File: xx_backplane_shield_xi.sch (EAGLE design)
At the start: 31 parts, among them U7 LM2678

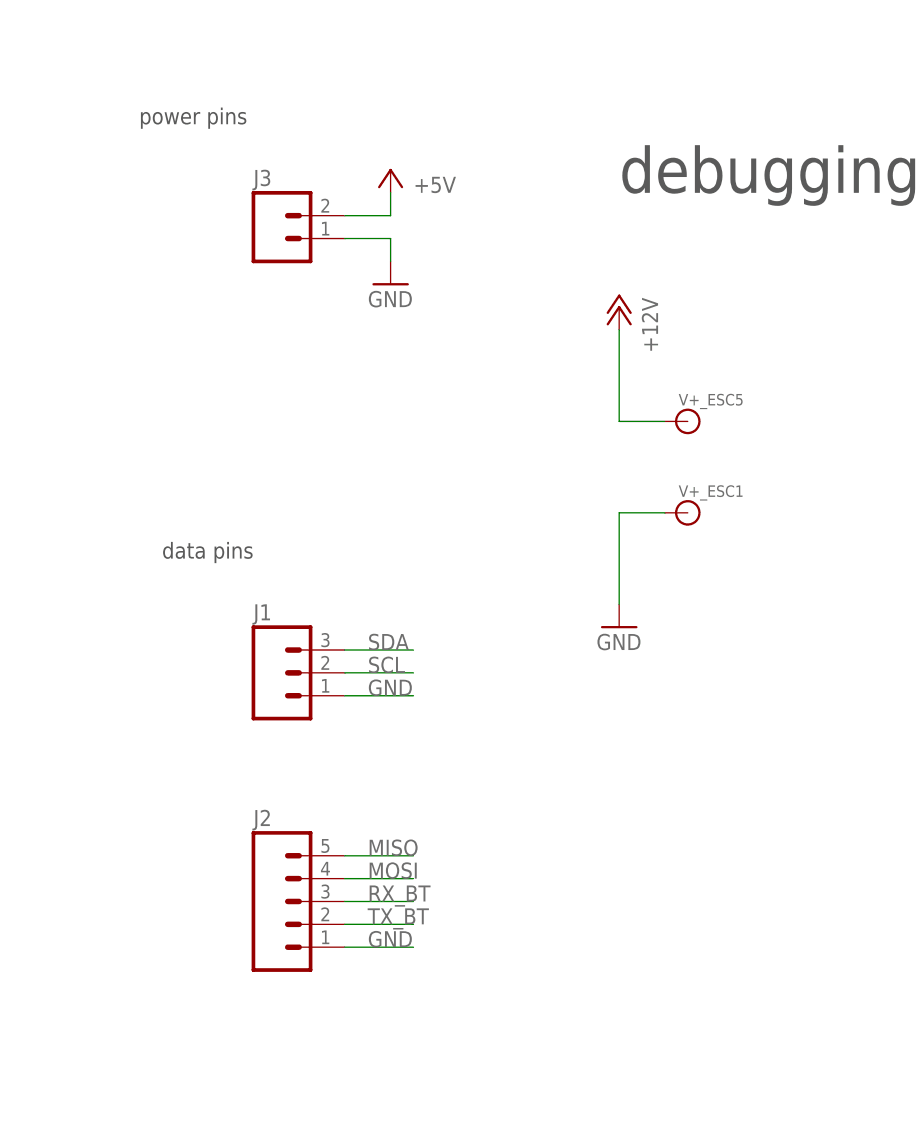
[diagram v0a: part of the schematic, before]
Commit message: Cleaning up eagle file and renaming board name
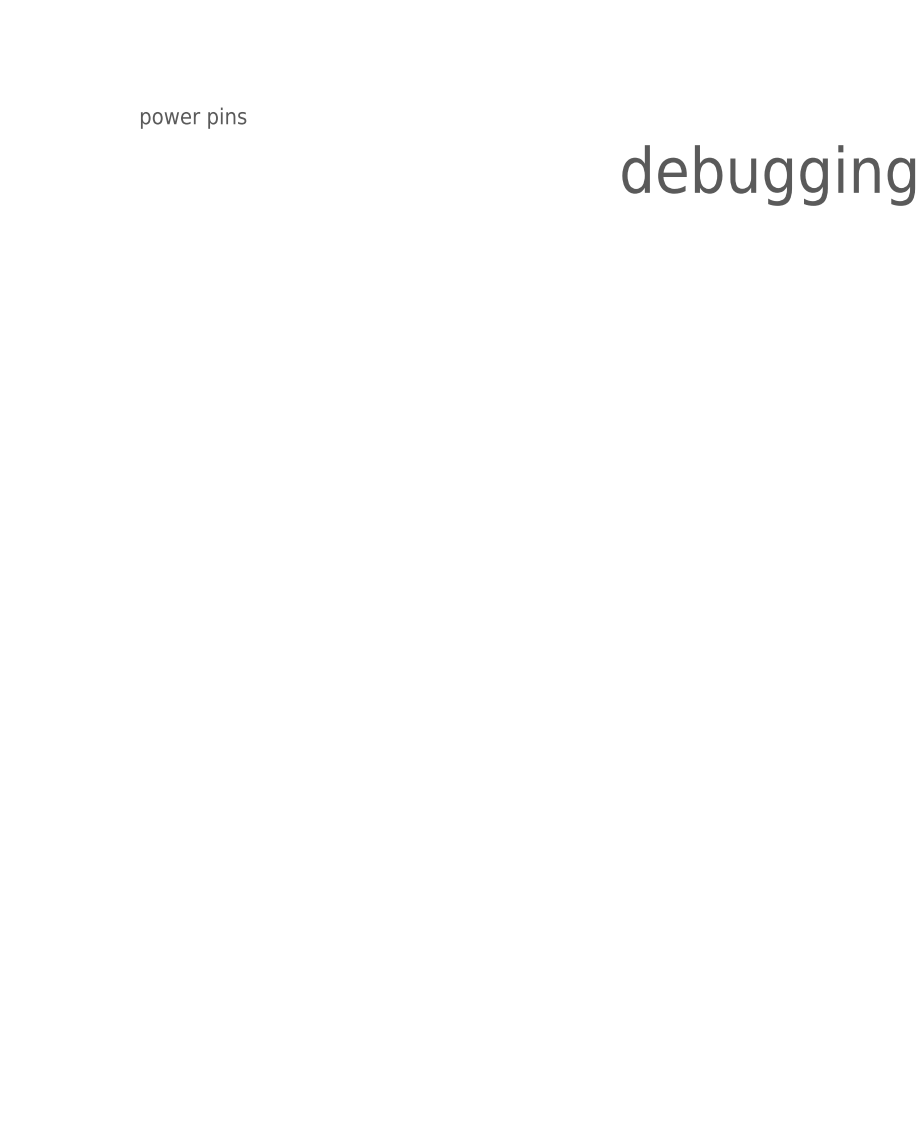
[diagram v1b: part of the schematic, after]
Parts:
- removed J1: (no value), SparkFun-Connectors:M03PTH
- removed J2: (no value), SparkFun-Connectors:M05PTH
- removed J3: (no value), SparkFun-Connectors:M02PTH
- removed V+_ESC1, V+_ESC5: (no value), SparkFun-Connectors:BANANA_CONN
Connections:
- removed net RX_BT: J2.3
- removed net TX_BT: J2.2
- net +12V: no longer V+_ESC5.1
- net +5V: no longer J3.2
- net GND: no longer J1.1, J2.1, J3.1, V+_ESC1.1
- net MISO: no longer J2.5
- net MOSI: no longer J2.4
- net SCL: no longer J1.2
- net SDA: no longer J1.3
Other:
- note removed: "data pins"
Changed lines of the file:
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@@
 <part name="GND19" library="SparkFun-Aesthetics" deviceset="GND" device=""/>
 <part name="P+3" library="supply1" deviceset="+12V" device=""/>
-<part name="J1" library="SparkFun-Connectors" deviceset="M03" device="PTH"/>
 <part name="FRAME5" library="frames" deviceset="FRAME_A_L" device=""/>
-<part name="J2" library="SparkFun-Connectors" deviceset="M05" device="PTH"/>
-<part name="J3" library="SparkFun-Connectors" deviceset="M02" device="PTH"/>
-<part name="P+8" library="supply1" deviceset="+5V" device=""/>
-<part name="GND25" library="SparkFun-Aesthetics" deviceset="GND" device=""/>
 <part name="C7" library="SparkFun-Passives" deviceset="CAP" device="0603-CAP" value="0.1u"/>
 <part name="GND29" library="SparkFun-Aesthetics" deviceset="GND" device=""/>
@@
 <part name="R14" library="resistor" deviceset="R-US_" device="R0603" value="330"/>
 <part name="GND33" library="SparkFun-Aesthetics" deviceset="GND" device=""/>
-<part name="P+10" library="supply1" deviceset="+12V" device=""/>
-<part name="GND34" library="SparkFun-Aesthetics" deviceset="GND" device=""/>
-<part name="V+_ESC5" library="SparkFun-Connectors" deviceset="BANANA_CONN" device=""/>
-<part name="V+_ESC1" library="SparkFun-Connectors" deviceset="BANANA_CONN" device=""/>
 <part name="C3" library="SparkFun-Capacitors" deviceset="0.18UF" device="-0603-10V-10%" value="0.47uF"/>
 </parts>
@@
 <text x="-40.64" y="177.8" size="5.08" layer="97">debugging pins</text>
 <text x="-93.98" y="185.42" size="1.778" layer="97">power pins</text>
-<text x="-91.44" y="137.16" size="1.778" layer="97">data pins</text>
 </plain>
 <instances>
@@
 <instance part="GND19" gate="1" x="-373.38" y="40.64"/>
 <instance part="P+3" gate="1" x="-373.38" y="81.28"/>
-<instance part="J1" gate="J$1" x="-78.74" y="124.46"/>
 <instance part="FRAME5" gate="G$1" x="-111.76" y="-22.86"/>
 <instance part="FRAME5" gate="G$2" x="60.96" y="-22.86"/>
-<instance part="J2" gate="G$1" x="-78.74" y="99.06"/>
-<instance part="J3" gate="G$1" x="-78.74" y="172.72"/>
-<instance part="P+8" gate="1" x="-66.04" y="180.34" smashed="yes">
-<attribute name="VALUE" x="-63.5" y="177.8" size="1.778" layer="96"/>
-</instance>
-<instance part="GND25" gate="1" x="-66.04" y="167.64"/>
 <instance part="C7" gate="G$1" x="-48.26" y="386.08" rot="R90"/>
 <instance part="GND29" gate="1" x="-40.64" y="381"/>
@@
 <instance part="R14" gate="G$1" x="-187.96" y="383.54" rot="R90"/>
 <instance part="GND33" gate="1" x="-187.96" y="358.14"/>
-<instance part="P+10" gate="1" x="-40.64" y="165.1" rot="MR0"/>
-<instance part="GND34" gate="1" x="-40.64" y="129.54"/>
-<instance part="V+_ESC5" gate="G$1" x="-33.02" y="152.4"/>
-<instance part="V+_ESC1" gate="G$1" x="-33.02" y="142.24"/>
 <instance part="C3" gate="G$1" x="-312.42" y="45.72"/>
 </instances>
@@
 </segment>
 <segment>
-<pinref part="J1" gate="J$1" pin="1"/>
-<wire x1="-71.12" y1="121.92" x2="-63.5" y2="121.92" width="0.1524" layer="91"/>
-<label x="-68.58" y="121.92" size="1.778" layer="95"/>
-</segment>
-<segment>
-<pinref part="J2" gate="G$1" pin="1"/>
-<wire x1="-71.12" y1="93.98" x2="-63.5" y2="93.98" width="0.1524" layer="91"/>
-<label x="-68.58" y="93.98" size="1.778" layer="95"/>
-</segment>
-<segment>
-<pinref part="J3" gate="G$1" pin="1"/>
-<wire x1="-71.12" y1="172.72" x2="-66.04" y2="172.72" width="0.1524" layer="91"/>
-<pinref part="GND25" gate="1" pin="GND"/>
-<wire x1="-66.04" y1="172.72" x2="-66.04" y2="170.18" width="0.1524" layer="91"/>
-</segment>
-<segment>
 <pinref part="C7" gate="G$1" pin="2"/>
 <pinref part="GND29" gate="1" pin="GND"/>
@@
 <pinref part="LED8" gate="G$1" pin="C"/>
 <wire x1="-187.96" y1="365.76" x2="-187.96" y2="360.68" width="0.1524" layer="91"/>
-</segment>
-<segment>
-<pinref part="GND34" gate="1" pin="GND"/>
-<wire x1="-40.64" y1="142.24" x2="-40.64" y2="132.08" width="0.1524" layer="91"/>
-<pinref part="V+_ESC1" gate="G$1" pin="1"/>
-<wire x1="-40.64" y1="142.24" x2="-35.56" y2="142.24" width="0.1524" layer="91"/>
 </segment>
 </net>
@@
 <wire x1="-373.38" y1="78.74" x2="-373.38" y2="73.66" width="0.1524" layer="91"/>
 </segment>
-<segment>
-<pinref part="P+10" gate="1" pin="+12V"/>
-<wire x1="-40.64" y1="152.4" x2="-40.64" y2="162.56" width="0.1524" layer="91"/>
-<pinref part="V+_ESC5" gate="G$1" pin="1"/>
-<wire x1="-40.64" y1="152.4" x2="-35.56" y2="152.4" width="0.1524" layer="91"/>
-</segment>
 </net>
 <net name="+5V" class="0">
@@
 <wire x1="-185.42" y1="63.5" x2="-185.42" y2="58.42" width="0.1524" layer="91"/>
 </segment>
-<segment>
-<pinref part="J3" gate="G$1" pin="2"/>
-<wire x1="-71.12" y1="175.26" x2="-66.04" y2="175.26" width="0.1524" layer="91"/>
-<pinref part="P+8" gate="1" pin="+5V"/>
-<wire x1="-66.04" y1="175.26" x2="-66.04" y2="177.8" width="0.1524" layer="91"/>
-</segment>
 </net>
 <net name="3.3V" class="0">
@@
 <label x="-317.5" y="241.3" size="1.778" layer="95"/>
 </segment>
-<segment>
-<pinref part="J1" gate="J$1" pin="3"/>
-<wire x1="-71.12" y1="127" x2="-63.5" y2="127" width="0.1524" layer="91"/>
-<label x="-68.58" y="127" size="1.778" layer="95"/>
-</segment>
 </net>
 <net name="SCL" class="0">
@@
 <wire x1="-322.58" y1="246.38" x2="-312.42" y2="246.38" width="0.1524" layer="91"/>
 <label x="-317.5" y="246.38" size="1.778" layer="95"/>
-</segment>
-<segment>
-<pinref part="J1" gate="J$1" pin="2"/>
-<wire x1="-71.12" y1="124.46" x2="-63.5" y2="124.46" width="0.1524" layer="91"/>
-<label x="-68.58" y="124.46" size="1.778" layer="95"/>
 </segment>
 </net>
@@
 </segment>
 </net>
-<net name="TX_BT" class="0">
-<segment>
-<pinref part="J2" gate="G$1" pin="2"/>
-<wire x1="-71.12" y1="96.52" x2="-63.5" y2="96.52" width="0.1524" layer="91"/>
-<label x="-68.58" y="96.52" size="1.778" layer="95"/>
-</segment>
-</net>
-<net name="RX_BT" class="0">
-<segment>
-<pinref part="J2" gate="G$1" pin="3"/>
-<wire x1="-71.12" y1="99.06" x2="-63.5" y2="99.06" width="0.1524" layer="91"/>
-<label x="-68.58" y="99.06" size="1.778" layer="95"/>
-</segment>
-</net>
 <net name="MISO" class="0">
 <segment>
@@
 <label x="-317.5" y="322.58" size="1.778" layer="95"/>
 </segment>
-<segment>
-<pinref part="J2" gate="G$1" pin="5"/>
-<wire x1="-71.12" y1="104.14" x2="-63.5" y2="104.14" width="0.1524" layer="91"/>
-<label x="-68.58" y="104.14" size="1.778" layer="95"/>
-</segment>
 </net>
 <net name="MOSI" class="0">
@@
 <label x="-368.3" y="327.66" size="1.778" layer="95"/>
 </segment>
-<segment>
-<pinref part="J2" gate="G$1" pin="4"/>
-<wire x1="-71.12" y1="101.6" x2="-63.5" y2="101.6" width="0.1524" layer="91"/>
-<label x="-68.58" y="101.6" size="1.778" layer="95"/>
-</segment>
-</net>
+</net>

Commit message: deleted like everything
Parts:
- removed C10, C6, C9: 150uF, PowerComponents:C-TANTALUM(10UF_150UF)
- removed C11, C12, C13, C2: 10uF, PowerComponents:C-TANTALUM(10UF_150UF)
- removed C3: 0.47uF, SparkFun-Capacitors:0.18UF-0603-10V-10%
- removed C4: 0.01uF, SparkFun-Passives:CAP0603-CAP
- removed LED4: (no value), led:LEDSML0603
- removed R2: 1k, resistor:R-US_R0603
- removed U$6: 15uH, DiscreteComponents:HCMA1305
- removed U7: LM2678, PowerComponents:LM2678
- added U$1: T2I, BackplaneParts:T2I
- U$2: value SWITCHMODE_SCHOTTKY -> T2I5P; device PowerComponents:SWITCHMODE_SCHOTTKY -> BackplaneParts:T2I5P
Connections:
- removed net +12V: C11.+, C12.+, C13.+, C2.+, C3.1, R2.2, U7.VIN
- removed net N$18: C4.1, U7.BOOST
- removed net N$19: C4.2, U$2.P$4, U$6.1, U7.OUTPUT
- removed net N$3: LED4.A, R2.1
- net +5V: now also U$2.4, U$2.5; no longer C10.+, C6.+, C9.+, U$6.2, U7.FEEDBACK
- net GND: now also U$2.1, U$2.2; no longer C10.-, C11.-, C12.-, C13.-, C2.-, C3.2, C6.-, C9.-, LED4.C, U$2.P$1, U$2.P$3, U7.GND, U7.TABGND
- net SCL: now also U$1.1
- net SDA: now also U$1.2

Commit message: finished board version 1
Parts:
- removed U$1: T2I, BackplaneParts:T2I
- added R2, R3: 330, resistor:R-US_R0603
- added U$4, U$6: THROUGHOLE, throughhole:THROUGHOLE
- U$2: value T2I5P -> T2I; device BackplaneParts:T2I5P -> BackplaneParts:T2I
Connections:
- removed net FIN: PCB1.GPIO13
- removed net LASER_ON: PCB1.GPIO5
- removed net MISO: PCB1.GPIO19
- removed net MOSI: PCB1.GPIO20
- removed net RX: PCB1.GPIO15
- removed net SCLK: PCB1.GPIO21
- removed net SERVO_PWM: PCB1.GPIO18
- removed net TX: PCB1.GPIO14
- net +5V: now also U$4.P$1; no longer U$2.5
- net 3.3V: now also R2.2, R3.2
- net GND: now also U$2.3, U$6.P$1; no longer U$2.1, U$2.2
- net LED1: now also PCB1.GPIO17; no longer PCB1.GPIO7
- net LED2: now also PCB1.GPIO27; no longer PCB1.GPIO8
- net LED3: now also PCB1.GPIO22; no longer PCB1.GPIO25
- net SCL: now also R3.1, U$2.2; no longer U$1.1
- net SDA: now also R2.1, U$2.1; no longer U$1.2
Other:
- note removed: "debugging pins"
- moved on the sheet: LED5, R1

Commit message: part placement almost done
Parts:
- removed LED6, LED7, LED8: (no value), led:LEDSML0603
- removed R12, R13, R14: 330, resistor:R-US_R0603
- added C1, C3: 0.1u, SparkFun-Passives:CAP0603-CAP
- added LED1, LED2, LED3, LED4: WS2812B5050, microbuilder:WS2812B5050
- added POWER: T2I5P, T2I5P:T2I5P
- added PS1, PS2: DF13-4P-1.25DSA, con-hirose-df13:DF13-4P-1.25DSA
- added R4, R6: 0 Ohms, resistor:R-US_R0603
- added R5, R7: 0 ohms, resistor:R-US_R0603
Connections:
- removed net BT_LED_ON: PCB1.GPIO16
- removed net LED_ON: PCB1.GPIO6
- removed net N$13: LED6.A, R12.1
- removed net N$14: LED7.A, R13.1
- removed net N$15: LED8.A, R14.1
- new net N$1: PS1.2, R4.2
- new net N$10: PS2.3, R7.2
- new net N$11: POWER.4
- new net N$12: POWER.5
- new net N$3: LED1.DO, LED2.DI
- new net N$4: LED2.DO, LED3.DI
- new net N$5: LED3.DO, LED4.DI
- new net N$8: PS1.3, R5.2
- new net N$9: PS2.2, R6.2
- new net NEO_PIXEL_IN: LED1.DI, PCB1.GPIO18
- net +5V: now also C1.1, C3.1, LED1.VDD, LED2.VDD, LED3.VDD, LED4.VDD; no longer U$2.4
- net 3.3V: now also PS1.1, PS2.1
- net GND: now also C1.2, C3.2, LED1.GND, LED2.GND, LED3.GND, LED4.GND, POWER.1, POWER.2, PS1.4, PS2.4; no longer LED6.C, LED7.C, LED8.C, U$2.3
- net LED1: no longer R12.2
- net LED2: no longer R13.2
- net LED3: no longer R14.2
- net SCL: now also R4.1, R6.1
- net SDA: now also R5.1, R7.1, U$2.3; no longer U$2.1
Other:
- moved on the sheet: C7, LED5, R1, R2, R3, U$2

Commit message: half way done routing first revision
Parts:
- removed R6: 0 Ohms, resistor:R-US_R0603
- removed R7: 0 ohms, resistor:R-US_R0603
- added USB_CAM_POW: (no value), pinhead:PINHD-1X3
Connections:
- removed net N$10: PS2.3, R7.2
- removed net N$11: POWER.4
- removed net N$12: POWER.5
- removed net N$9: PS2.2, R6.2
- net +5V: now also POWER.4, POWER.5, USB_CAM_POW.1
- net GND: now also USB_CAM_POW.3
- net SCL: now also PS2.2; no longer R6.1
- net SDA: now also PS2.3; no longer R7.1
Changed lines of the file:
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@@
 <part name="R5" library="resistor" library_urn="urn:adsk.eagle:library:348" deviceset="R-US_" device="R0603" package3d_urn="urn:adsk.eagle:package:26057/1" value="0 ohms"/>
 <part name="PS2" library="con-hirose-df13" deviceset="DF13-4P-1.25" device="DSA"/>
-<part name="R6" library="resistor" library_urn="urn:adsk.eagle:library:348" deviceset="R-US_" device="R0603" package3d_urn="urn:adsk.eagle:package:26057/1" value="0 Ohms"/>
-<part name="R7" library="resistor" library_urn="urn:adsk.eagle:library:348" deviceset="R-US_" device="R0603" package3d_urn="urn:adsk.eagle:package:26057/1" value="0 ohms"/>
+<part name="USB_CAM_POW" library="pinhead" library_urn="urn:adsk.eagle:library:325" deviceset="PINHD-1X3" device="" package3d_urn="urn:adsk.eagle:package:22458/2"/>
 </parts>
 <sheets>
@@
 <attribute name="NAME" x="-52.705" y="134.62" size="1.778" layer="95"/>
 </instance>
-<instance part="R6" gate="G$1" x="-63.5" y="129.54" smashed="yes">
-<attribute name="NAME" x="-67.31" y="131.0386" size="1.778" layer="95"/>
-</instance>
-<instance part="R7" gate="G$1" x="-68.58" y="127" smashed="yes">
-<attribute name="NAME" x="-72.39" y="128.4986" size="1.778" layer="95"/>
-</instance>
+<instance part="USB_CAM_POW" gate="A" x="-48.26" y="58.42"/>
 </instances>
 <busses>
@@
 <pinref part="POWER" gate="&gt;NAME" pin="1"/>
 <wire x1="-58.42" y1="86.36" x2="-66.04" y2="86.36" width="0.1524" layer="91"/>
+<label x="-66.04" y="86.36" size="1.778" layer="95"/>
 </segment>
 <segment>
 <pinref part="POWER" gate="&gt;NAME" pin="2"/>
 <wire x1="-58.42" y1="83.82" x2="-66.04" y2="83.82" width="0.1524" layer="91"/>
+<label x="-66.04" y="83.82" size="1.778" layer="95"/>
+</segment>
+<segment>
+<pinref part="USB_CAM_POW" gate="A" pin="3"/>
+<wire x1="-50.8" y1="55.88" x2="-66.04" y2="55.88" width="0.1524" layer="91"/>
+<label x="-66.04" y="55.88" size="1.778" layer="95"/>
 </segment>
 </net>
@@
 <junction x="127" y="129.54"/>
 </segment>
+<segment>
+<pinref part="POWER" gate="&gt;NAME" pin="4"/>
+<wire x1="-58.42" y1="78.74" x2="-66.04" y2="78.74" width="0.1524" layer="91"/>
+<label x="-66.04" y="78.74" size="1.778" layer="95"/>
+</segment>
+<segment>
+<pinref part="POWER" gate="&gt;NAME" pin="5"/>
+<wire x1="-58.42" y1="76.2" x2="-66.04" y2="76.2" width="0.1524" layer="91"/>
+<label x="-66.04" y="76.2" size="1.778" layer="95"/>
+</segment>
+<segment>
+<pinref part="USB_CAM_POW" gate="A" pin="1"/>
+<wire x1="-50.8" y1="60.96" x2="-66.04" y2="60.96" width="0.1524" layer="91"/>
+<label x="-66.04" y="60.96" size="1.778" layer="95"/>
+</segment>
 </net>
 <net name="3.3V" class="0">
@@
 </segment>
 <segment>
-<pinref part="R7" gate="G$1" pin="1"/>
-<wire x1="-73.66" y1="127" x2="-81.28" y2="127" width="0.1524" layer="91"/>
 <label x="-81.28" y="127" size="1.778" layer="95"/>
+<pinref part="PS2" gate="G$1" pin="3"/>
+<wire x1="-81.28" y1="127" x2="-55.88" y2="127" width="0.1524" layer="91"/>
 </segment>
 </net>
@@
 </segment>
 <segment>
-<pinref part="R6" gate="G$1" pin="1"/>
-<wire x1="-68.58" y1="129.54" x2="-81.28" y2="129.54" width="0.1524" layer="91"/>
+<wire x1="-55.88" y1="129.54" x2="-81.28" y2="129.54" width="0.1524" layer="91"/>
 <label x="-81.28" y="129.54" size="1.778" layer="95"/>
+<pinref part="PS2" gate="G$1" pin="2"/>
 </segment>
 </net>
@@
 </segment>
 </net>
-<net name="N$9" class="0">
-<segment>
-<pinref part="PS2" gate="G$1" pin="2"/>
-<pinref part="R6" gate="G$1" pin="2"/>
-<wire x1="-55.88" y1="129.54" x2="-58.42" y2="129.54" width="0.1524" layer="91"/>
-</segment>
-</net>
-<net name="N$10" class="0">
-<segment>
-<pinref part="PS2" gate="G$1" pin="3"/>
-<pinref part="R7" gate="G$1" pin="2"/>
-<wire x1="-55.88" y1="127" x2="-63.5" y2="127" width="0.1524" layer="91"/>
-</segment>
-</net>
-<net name="N$11" class="0">
-<segment>
-<pinref part="POWER" gate="&gt;NAME" pin="4"/>
-<wire x1="-58.42" y1="78.74" x2="-66.04" y2="78.74" width="0.1524" layer="91"/>
-</segment>
-</net>
-<net name="N$12" class="0">
-<segment>
-<pinref part="POWER" gate="&gt;NAME" pin="5"/>
-<wire x1="-58.42" y1="76.2" x2="-66.04" y2="76.2" width="0.1524" layer="91"/>
-</segment>
-</net>

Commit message: made the fixes
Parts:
- added C2, C4: 0.1u, SparkFun-Passives:CAP0603-CAP
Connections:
- net +5V: now also C2.1, C4.1
- net GND: now also C2.2, C4.2
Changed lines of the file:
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@@
 <part name="PS2" library="con-hirose-df13" deviceset="DF13-4P-1.25" device="DSA"/>
 <part name="USB_CAM_POW" library="pinhead" library_urn="urn:adsk.eagle:library:325" deviceset="PINHD-1X3" device="" package3d_urn="urn:adsk.eagle:package:22458/2"/>
+<part name="C2" library="SparkFun-Passives" deviceset="CAP" device="0603-CAP" value="0.1u"/>
+<part name="C4" library="SparkFun-Passives" deviceset="CAP" device="0603-CAP" value="0.1u"/>
+<part name="GND7" library="SparkFun-Aesthetics" deviceset="GND" device=""/>
+<part name="GND14" library="SparkFun-Aesthetics" deviceset="GND" device=""/>
 </parts>
 <sheets>
@@
 </instance>
 <instance part="USB_CAM_POW" gate="A" x="-48.26" y="58.42"/>
+<instance part="C2" gate="G$1" x="96.52" y="121.92"/>
+<instance part="C4" gate="G$1" x="157.48" y="121.92"/>
+<instance part="GND7" gate="1" x="96.52" y="114.3"/>
+<instance part="GND14" gate="1" x="157.48" y="114.3"/>
 </instances>
 <busses>
@@
 <label x="-66.04" y="55.88" size="1.778" layer="95"/>
 </segment>
+<segment>
+<pinref part="C2" gate="G$1" pin="2"/>
+<pinref part="GND7" gate="1" pin="GND"/>
+<wire x1="96.52" y1="119.38" x2="96.52" y2="116.84" width="0.1524" layer="91"/>
+</segment>
+<segment>
+<pinref part="C4" gate="G$1" pin="2"/>
+<pinref part="GND14" gate="1" pin="GND"/>
+<wire x1="157.48" y1="119.38" x2="157.48" y2="116.84" width="0.1524" layer="91"/>
+</segment>
 </net>
 <net name="+5V" class="0">
@@
 <wire x1="86.36" y1="129.54" x2="86.36" y2="119.38" width="0.1524" layer="91"/>
 <pinref part="LED3" gate="G$1" pin="VDD"/>
-<wire x1="86.36" y1="129.54" x2="116.84" y2="129.54" width="0.1524" layer="91"/>
+<wire x1="86.36" y1="129.54" x2="96.52" y2="129.54" width="0.1524" layer="91"/>
+<wire x1="96.52" y1="129.54" x2="116.84" y2="129.54" width="0.1524" layer="91"/>
 <wire x1="116.84" y1="129.54" x2="116.84" y2="119.38" width="0.1524" layer="91"/>
 <junction x="86.36" y="129.54"/>
@@
 <wire x1="127" y1="127" x2="127" y2="129.54" width="0.1524" layer="91"/>
 <junction x="127" y="129.54"/>
-</segment>
-<segment>
+<pinref part="C2" gate="G$1" pin="1"/>
+<wire x1="96.52" y1="127" x2="96.52" y2="129.54" width="0.1524" layer="91"/>
+<junction x="96.52" y="129.54"/>
+<pinref part="C4" gate="G$1" pin="1"/>
+<wire x1="157.48" y1="127" x2="157.48" y2="129.54" width="0.1524" layer="91"/>
+<wire x1="157.48" y1="129.54" x2="147.32" y2="129.54" width="0.1524" layer="91"/>
+<junction x="147.32" y="129.54"/>
+</segment>
+<segment>
